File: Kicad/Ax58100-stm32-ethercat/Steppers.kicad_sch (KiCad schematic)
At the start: 13 parts, among them J11 Conn_01x03, J13 Conn_01x03, J17 THCAD, J7 Conn_01x05, U11 MAX3485, U9 TXB0104PW

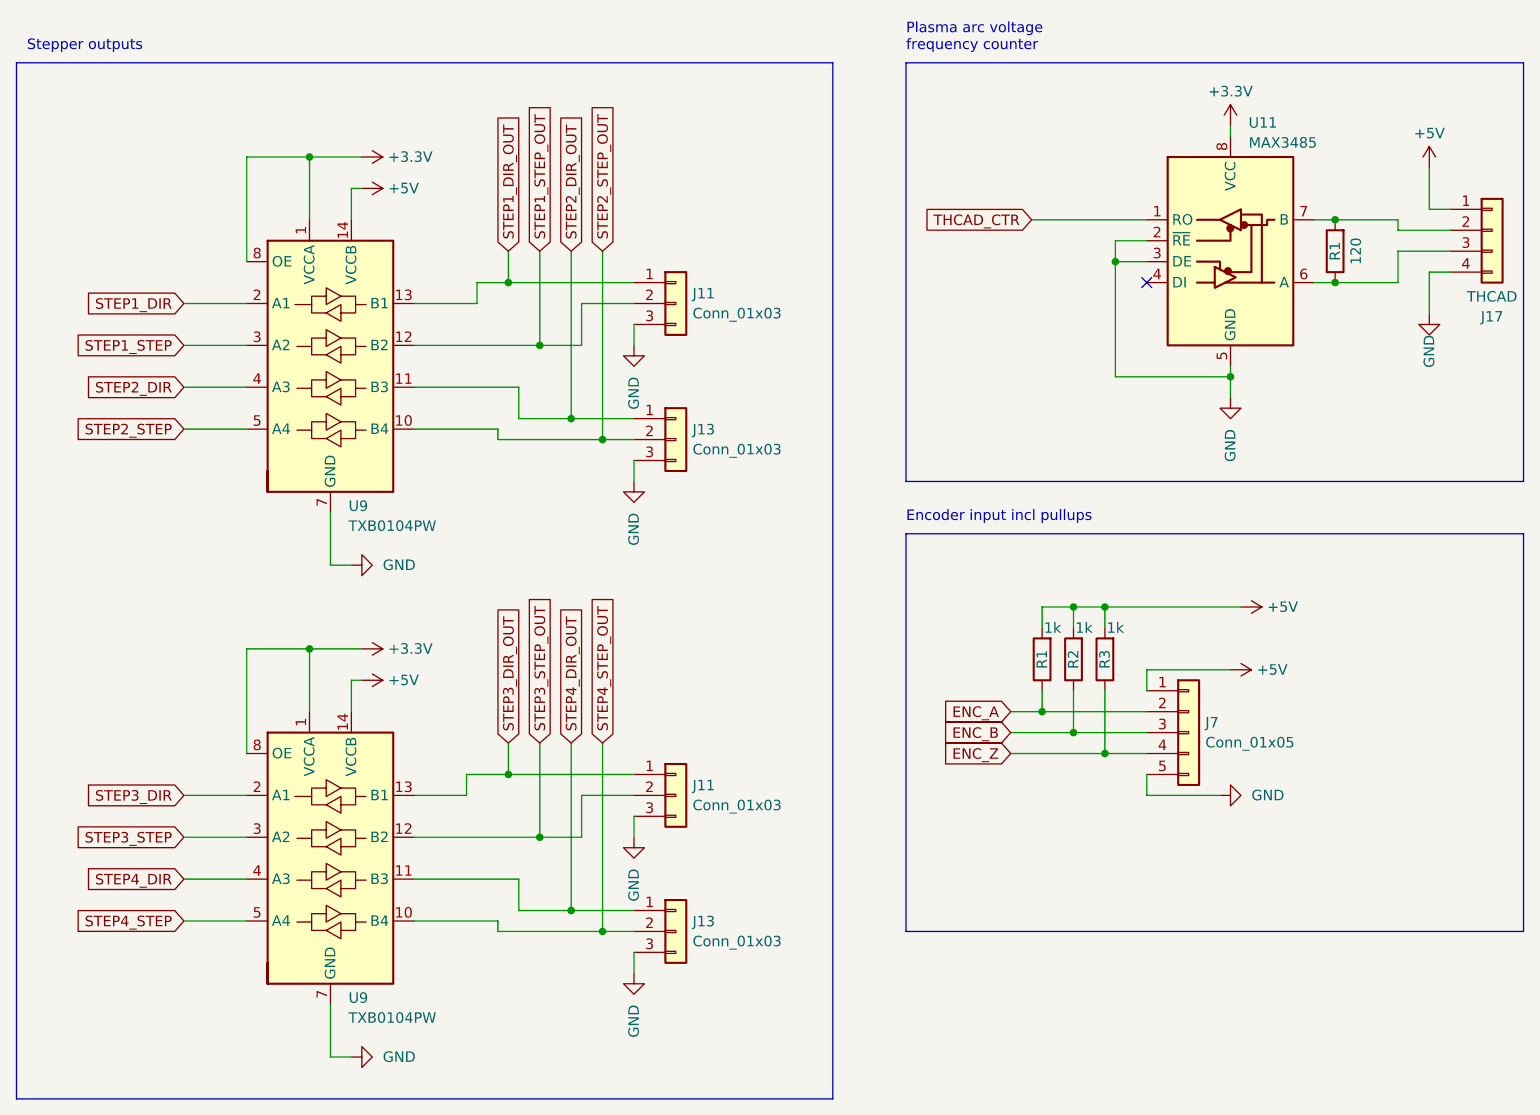
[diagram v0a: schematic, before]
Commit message: Assigned footprints
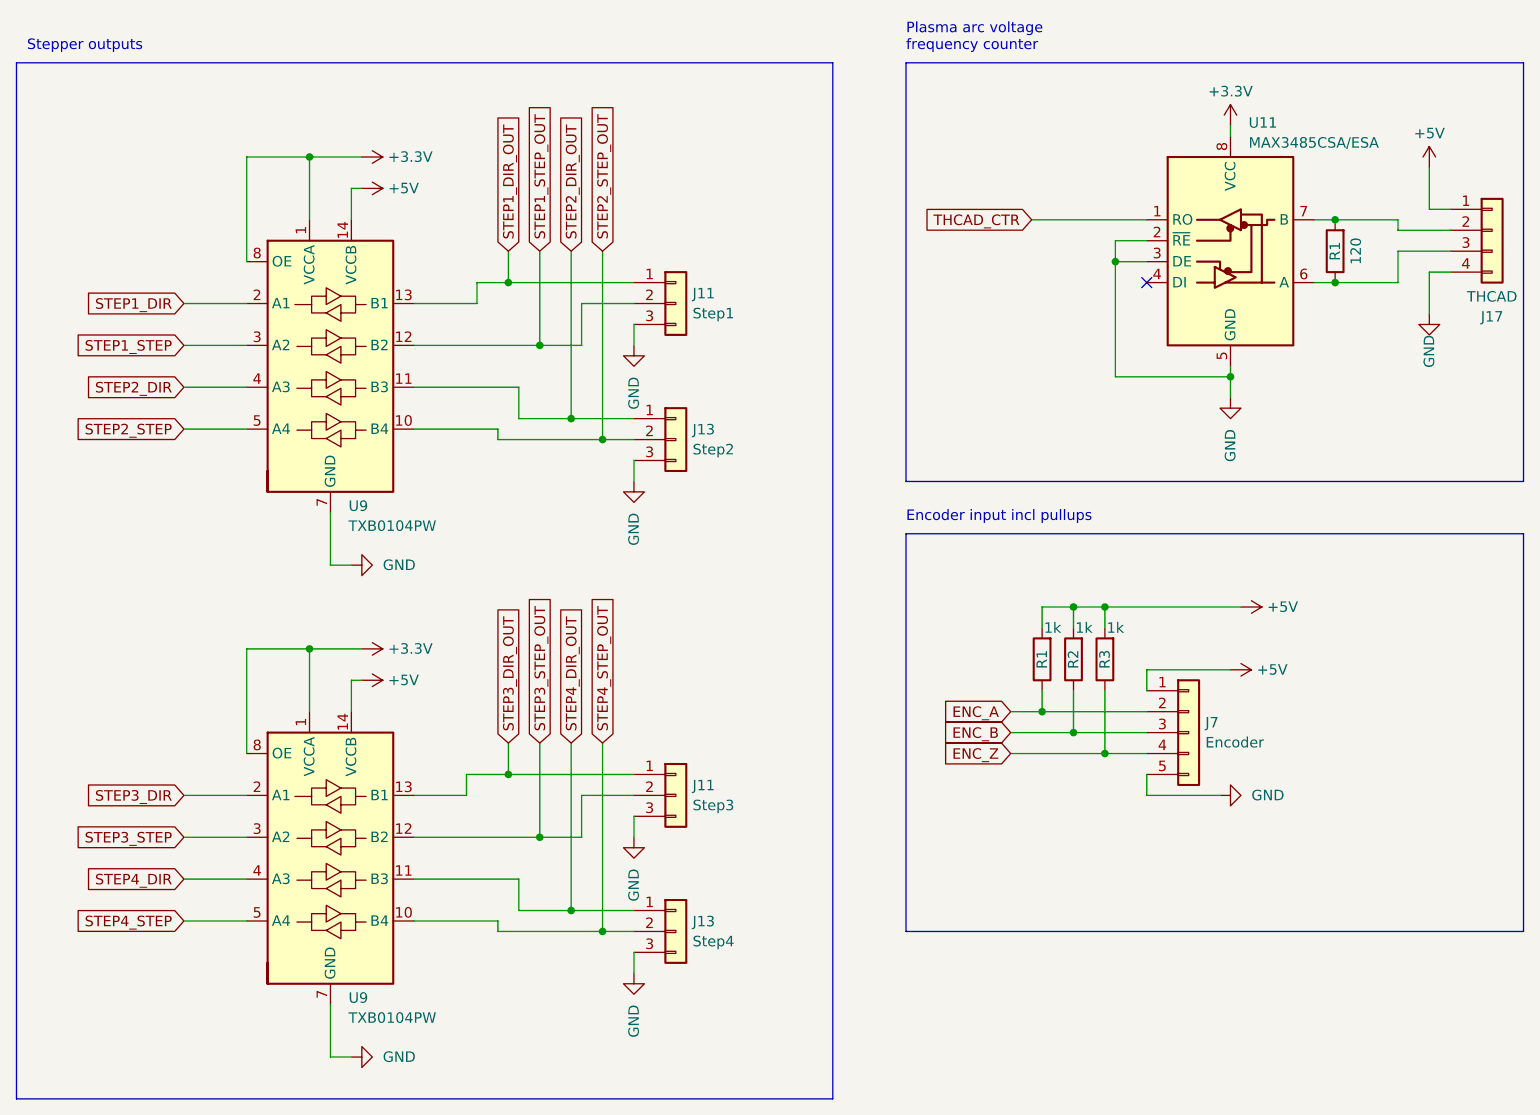
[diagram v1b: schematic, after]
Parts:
- J11: value Conn_01x03 -> Step1; footprint (none) -> TerminalBlock:TerminalBlock_bornier-3_P5.08mm
- J11: value Conn_01x03 -> Step3; footprint (none) -> TerminalBlock:TerminalBlock_bornier-3_P5.08mm
- J13: value Conn_01x03 -> Step2; footprint (none) -> TerminalBlock:TerminalBlock_bornier-3_P5.08mm
- J13: value Conn_01x03 -> Step4; footprint (none) -> TerminalBlock:TerminalBlock_bornier-3_P5.08mm
- J17: footprint (none) -> TerminalBlock:TerminalBlock_bornier-4_P5.08mm
- J7: value Conn_01x05 -> Encoder; footprint (none) -> TerminalBlock:TerminalBlock_bornier-5_P5.08mm
- U11: value MAX3485 -> MAX3485CSA/ESA; footprint (none) -> Package_SO:SO-8_3.9x4.9mm_P1.27mm
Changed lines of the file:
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@@
       (effects (font (size 1.27 1.27)))
     )
-    (property "Footprint" "" (at 212.09 54.61 0)
+    (property "Footprint" "TerminalBlock:TerminalBlock_bornier-4_P5.08mm" (at 212.09 54.61 0)
       (effects (font (size 1.27 1.27)) hide)
     )
@@
       (effects (font (size 1.27 1.27)) (justify left))
     )
-    (property "Value" "Conn_01x03" (at 115.062 81.2221 0)
-      (effects (font (size 1.27 1.27)) (justify left))
-    )
-    (property "Footprint" "" (at 113.03 80.01 0)
+    (property "Value" "Step2" (at 115.062 81.2221 0)
+      (effects (font (size 1.27 1.27)) (justify left))
+    )
+    (property "Footprint" "TerminalBlock:TerminalBlock_bornier-3_P5.08mm" (at 113.03 80.01 0)
       (effects (font (size 1.27 1.27)) hide)
     )
@@
       (effects (font (size 1.27 1.27)) (justify left))
     )
-    (property "Value" "MAX3485" (at 182.5341 43.9999 0)
-      (effects (font (size 1.27 1.27)) (justify left))
-    )
-    (property "Footprint" "" (at 180.34 73.66 0)
+    (property "Value" "MAX3485CSA/ESA" (at 182.5341 43.9999 0)
+      (effects (font (size 1.27 1.27)) (justify left))
+    )
+    (property "Footprint" "Package_SO:SO-8_3.9x4.9mm_P1.27mm" (at 180.34 73.66 0)
       (effects (font (size 1.27 1.27)) hide)
     )
@@
       (effects (font (size 1.27 1.27)) (justify left))
     )
-    (property "Value" "Conn_01x03" (at 115.062 64.7121 0)
-      (effects (font (size 1.27 1.27)) (justify left))
-    )
-    (property "Footprint" "" (at 113.03 63.5 0)
+    (property "Value" "Step1" (at 115.062 64.7121 0)
+      (effects (font (size 1.27 1.27)) (justify left))
+    )
+    (property "Footprint" "TerminalBlock:TerminalBlock_bornier-3_P5.08mm" (at 113.03 63.5 0)
       (effects (font (size 1.27 1.27)) hide)
     )
@@
       (effects (font (size 1.27 1.27)) (justify left))
     )
-    (property "Value" "Conn_01x05" (at 177.292 116.7821 0)
-      (effects (font (size 1.27 1.27)) (justify left))
-    )
-    (property "Footprint" "" (at 175.26 115.57 0)
+    (property "Value" "Encoder" (at 177.292 116.7821 0)
+      (effects (font (size 1.27 1.27)) (justify left))
+    )
+    (property "Footprint" "TerminalBlock:TerminalBlock_bornier-5_P5.08mm" (at 175.26 115.57 0)
       (effects (font (size 1.27 1.27)) hide)
     )
@@
       (effects (font (size 1.27 1.27)) (justify left))
     )
-    (property "Value" "Conn_01x03" (at 115.062 124.4021 0)
-      (effects (font (size 1.27 1.27)) (justify left))
-    )
-    (property "Footprint" "" (at 113.03 123.19 0)
+    (property "Value" "Step3" (at 115.062 124.4021 0)
+      (effects (font (size 1.27 1.27)) (justify left))
+    )
+    (property "Footprint" "TerminalBlock:TerminalBlock_bornier-3_P5.08mm" (at 113.03 123.19 0)
       (effects (font (size 1.27 1.27)) hide)
     )
@@
       (effects (font (size 1.27 1.27)) (justify left))
     )
-    (property "Value" "Conn_01x03" (at 115.062 140.9121 0)
-      (effects (font (size 1.27 1.27)) (justify left))
-    )
-    (property "Footprint" "" (at 113.03 139.7 0)
-      (effects (font (size 1.27 1.27)) hide)
-    )
+    (property "Value" "Step4" (at 115.062 140.9121 0)
+      (effects (font (size 1.27 1.27)) (justify left))
+    )
+    (property "Footprint" "TerminalBlock:TerminalBlock_bornier-3_P5.08mm" (at 113.03 139.7 0)
+      (effects (font (size 1.27 1.27)) hide)
+    )

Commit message: First component placement
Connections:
- net at R1.1, U11.6 (A): now also J17.2 (Pin_2); no longer J17.3 (Pin_3)
- net at R1.2, U11.7 (B): now also J17.3 (Pin_3); no longer J17.2 (Pin_2)
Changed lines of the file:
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@@
   )
   (no_connect (at 170.18 60.96))
-  (wire (pts (xy 204.47 52.07) (xy 204.47 46.99))
+  (wire (pts (xy 204.47 59.69) (xy 204.47 64.77))
     (stroke (width 0) (type default))
   )
@@
     (stroke (width 0) (type default))
   )
+  (wire (pts (xy 204.47 52.07) (xy 207.01 52.07))
+    (stroke (width 0) (type default))
+  )
+  (wire (pts (xy 71.12 95.25) (xy 71.12 88.9))
+    (stroke (width 0) (type default))
+  )
+  (wire (pts (xy 68.58 45.72) (xy 60.96 45.72))
+    (stroke (width 0) (type default))
+  )
+  (wire (pts (xy 71.12 154.94) (xy 73.66 154.94))
+    (stroke (width 0) (type default))
+  )
+  (wire (pts (xy 53.34 63.5) (xy 60.96 63.5))
+    (stroke (width 0) (type default))
+  )
+  (wire (pts (xy 180.34 72.39) (xy 180.34 71.12))
+    (stroke (width 0) (type default))
+  )
+  (wire (pts (xy 107.95 66.04) (xy 107.95 68.58))
+    (stroke (width 0) (type default))
+  )
+  (wire (pts (xy 190.5 53.34) (xy 193.04 53.34))
+    (stroke (width 0) (type default))
+  )
+  (wire (pts (xy 180.34 107.95) (xy 170.18 107.95))
+    (stroke (width 0) (type default))
+  )
+  (wire (pts (xy 53.34 138.43) (xy 60.96 138.43))
+    (stroke (width 0) (type default))
+  )
+  (wire (pts (xy 166.37 72.39) (xy 180.34 72.39))
+    (stroke (width 0) (type default))
+  )
+  (wire (pts (xy 161.29 100.33) (xy 161.29 102.87))
+    (stroke (width 0) (type default))
+  )
+  (wire (pts (xy 71.12 154.94) (xy 71.12 148.59))
+    (stroke (width 0) (type default))
+  )
+  (wire (pts (xy 101.6 63.5) (xy 107.95 63.5))
+    (stroke (width 0) (type default))
+  )
+  (wire (pts (xy 170.18 107.95) (xy 170.18 110.49))
+    (stroke (width 0) (type default))
+  )
+  (wire (pts (xy 104.14 80.01) (xy 107.95 80.01))
+    (stroke (width 0) (type default))
+  )
+  (wire (pts (xy 166.37 55.88) (xy 170.18 55.88))
+    (stroke (width 0) (type default))
+  )
   (wire (pts (xy 204.47 59.69) (xy 207.01 59.69))
     (stroke (width 0) (type default))
   )
-  (wire (pts (xy 71.12 95.25) (xy 71.12 88.9))
-    (stroke (width 0) (type default))
-  )
-  (wire (pts (xy 68.58 45.72) (xy 60.96 45.72))
-    (stroke (width 0) (type default))
-  )
-  (wire (pts (xy 71.12 154.94) (xy 73.66 154.94))
-    (stroke (width 0) (type default))
-  )
-  (wire (pts (xy 53.34 63.5) (xy 60.96 63.5))
-    (stroke (width 0) (type default))
-  )
-  (wire (pts (xy 180.34 72.39) (xy 180.34 71.12))
-    (stroke (width 0) (type default))
-  )
-  (wire (pts (xy 107.95 66.04) (xy 107.95 68.58))
-    (stroke (width 0) (type default))
-  )
-  (wire (pts (xy 190.5 53.34) (xy 193.04 53.34))
-    (stroke (width 0) (type default))
-  )
-  (wire (pts (xy 180.34 107.95) (xy 170.18 107.95))
-    (stroke (width 0) (type default))
-  )
-  (wire (pts (xy 53.34 138.43) (xy 60.96 138.43))
-    (stroke (width 0) (type default))
-  )
-  (wire (pts (xy 166.37 72.39) (xy 180.34 72.39))
-    (stroke (width 0) (type default))
-  )
-  (wire (pts (xy 161.29 100.33) (xy 161.29 102.87))
-    (stroke (width 0) (type default))
-  )
-  (wire (pts (xy 71.12 154.94) (xy 71.12 148.59))
-    (stroke (width 0) (type default))
-  )
-  (wire (pts (xy 101.6 63.5) (xy 107.95 63.5))
-    (stroke (width 0) (type default))
-  )
-  (wire (pts (xy 170.18 107.95) (xy 170.18 110.49))
-    (stroke (width 0) (type default))
-  )
-  (wire (pts (xy 104.14 80.01) (xy 107.95 80.01))
-    (stroke (width 0) (type default))
-  )
-  (wire (pts (xy 166.37 55.88) (xy 170.18 55.88))
-    (stroke (width 0) (type default))
-  )
-  (wire (pts (xy 204.47 52.07) (xy 207.01 52.07))
-    (stroke (width 0) (type default))
-  )
   (wire (pts (xy 193.04 60.96) (xy 200.66 60.96))
     (stroke (width 0) (type default))
@@
     (stroke (width 0) (type default))
   )
-  (wire (pts (xy 204.47 64.77) (xy 204.47 59.69))
+  (wire (pts (xy 204.47 46.99) (xy 204.47 52.07))
     (stroke (width 0) (type default))
   )
@@
     )
   )
-  (symbol (lib_id "Connector_Generic:Conn_01x04") (at 212.09 54.61 0) (unit 1)
+  (symbol (lib_id "Connector_Generic:Conn_01x04") (at 212.09 57.15 0) (mirror x) (unit 1)
     (in_bom yes) (on_board yes) (dnp no)
-    (property "Reference" "J17" (at 212.09 65.1043 0)
+    (property "Reference" "J17" (at 212.09 46.6557 0)
       (effects (font (size 1.27 1.27)))
     )
-    (property "Value" "THCAD" (at 212.09 62.6801 0)
+    (property "Value" "THCAD" (at 212.09 49.0799 0)
       (effects (font (size 1.27 1.27)))
     )
-    (property "Footprint" "TerminalBlock:TerminalBlock_bornier-4_P5.08mm" (at 212.09 54.61 0)
-      (effects (font (size 1.27 1.27)) hide)
-    )
-    (property "Datasheet" "~" (at 212.09 54.61 0)
+    (property "Footprint" "TerminalBlock:TerminalBlock_bornier-4_P5.08mm" (at 212.09 57.15 0)
+      (effects (font (size 1.27 1.27)) hide)
+    )
+    (property "Datasheet" "~" (at 212.09 57.15 0)
       (effects (font (size 1.27 1.27)) hide)
     )
@@
     )
   )
-  (symbol (lib_id "power:+5V") (at 204.47 46.99 0) (unit 1)
+  (symbol (lib_id "power:+5V") (at 204.47 64.77 0) (mirror x) (unit 1)
     (in_bom yes) (on_board yes) (dnp no) (fields_autoplaced)
-    (property "Reference" "#PWR?" (at 204.47 50.8 0)
-      (effects (font (size 1.27 1.27)) hide)
-    )
-    (property "Value" "+5V" (at 204.47 42.8569 0)
+    (property "Reference" "#PWR?" (at 204.47 60.96 0)
+      (effects (font (size 1.27 1.27)) hide)
+    )
+    (property "Value" "+5V" (at 204.47 68.9031 0)
       (effects (font (size 1.27 1.27)))
     )
-    (property "Footprint" "" (at 204.47 46.99 0)
-      (effects (font (size 1.27 1.27)) hide)
-    )
-    (property "Datasheet" "" (at 204.47 46.99 0)
+    (property "Footprint" "" (at 204.47 64.77 0)
+      (effects (font (size 1.27 1.27)) hide)
+    )
+    (property "Datasheet" "" (at 204.47 64.77 0)
       (effects (font (size 1.27 1.27)) hide)
     )
@@
     )
   )
-  (symbol (lib_id "power:GND") (at 204.47 64.77 0) (unit 1)
+  (symbol (lib_id "power:GND") (at 204.47 46.99 0) (mirror x) (unit 1)
     (in_bom yes) (on_board yes) (dnp no)
-    (property "Reference" "#PWR?" (at 204.47 71.12 0)
-      (effects (font (size 1.27 1.27)) hide)
-    )
-    (property "Value" "GND" (at 204.47 67.31 90)
+    (property "Reference" "#PWR?" (at 204.47 40.64 0)
+      (effects (font (size 1.27 1.27)) hide)
+    )
+    (property "Value" "GND" (at 204.47 44.45 90)
       (effects (font (size 1.27 1.27)) (justify right))
     )
-    (property "Footprint" "" (at 204.47 64.77 0)
-      (effects (font (size 1.27 1.27)) hide)
-    )
-    (property "Datasheet" "" (at 204.47 64.77 0)
-      (effects (font (size 1.27 1.27)) hide)
-    )
+    (property "Footprint" "" (at 204.47 46.99 0)
+      (effects (font (size 1.27 1.27)) hide)
+    )
+    (property "Datasheet" "" (at 204.47 46.99 0)
+      (effects (font (size 1.27 1.27)) hide)
+    )

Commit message: wip
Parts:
- removed U9 (x2): TXB0104PW, Package_SO:TSSOP-14_4.4x5mm_P0.65mm, symbol Logic_LevelTranslator:TXB0104PW
- added C34 (x3): 0.1uF, Capacitor_SMD:C_0805_2012Metric, symbol Device:C
- added U12: TXS0108EPW, Package_SO:TSSOP-20_4.4x6.5mm_P0.65mm, symbol Logic_LevelTranslator:TXS0108EPW
- renumbered J7 to J13, U11 to U3
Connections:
- net +3.3V: now also C34.1, C34.1, U12.10 (OE), U12.2 (VCCA)
- net +5V: now also C34.1, U12.19 (VCCB)
- net GND: now also C34.2, C34.2, C34.2, U12.11 (GND)
- net STEP1_DIR: now also U12.1 (A1)
- net STEP1_DIR_OUT: now also U12.20 (B1)
- net STEP1_STEP: now also U12.3 (A2)
- net STEP1_STEP_OUT: now also U12.18 (B2)
- net STEP2_DIR: now also U12.4 (A3)
- net STEP2_DIR_OUT: now also U12.17 (B3)
- net STEP2_STEP: now also U12.5 (A4)
- net STEP2_STEP_OUT: now also U12.16 (B4)
- net STEP3_DIR: now also U12.6 (A5)
- net STEP3_DIR_OUT: now also U12.15 (B5)
- net STEP3_STEP: now also U12.7 (A6)
- net STEP3_STEP_OUT: now also U12.14 (B6)
- net STEP4_DIR: now also U12.8 (A7)
- net STEP4_DIR_OUT: now also U12.13 (B7)
- net STEP4_STEP: now also U12.9 (A8)
- net STEP4_STEP_OUT: now also U12.12 (B8)
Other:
- moved on the sheet: J11, J13

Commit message: Might be in final shape.
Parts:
- J10: renamed from J13; footprint TerminalBlock:TerminalBlock_bornier-5_P5.08mm -> Connector_Phoenix_MC:PhoenixContact_MCV_1,5_5-G-3.5_1x05_P3.50mm_Vertical
- J11, J13: footprint TerminalBlock:TerminalBlock_bornier-3_P5.08mm -> Connector_Phoenix_MC:PhoenixContact_MCV_1,5_3-G-3.5_1x03_P3.50mm_Vertical
- J17: footprint TerminalBlock:TerminalBlock_bornier-4_P5.08mm -> Connector_Phoenix_MC:PhoenixContact_MCV_1,5_4-G-3.5_1x04_P3.50mm_Vertical
- renumbered U3 to U1, U12 to U2
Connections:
- net at R1.1, U1.6 (A): now also J17.3 (Pin_3); no longer J17.2 (Pin_2)
- net at R1.2, U1.7 (B): now also J17.2 (Pin_2); no longer J17.3 (Pin_3)
